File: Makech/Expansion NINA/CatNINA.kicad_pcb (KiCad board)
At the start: 2 copper layers, 22.9 x 30.9 mm, 10 parts, among them J1 ESP, U1 ESP32-WROOM

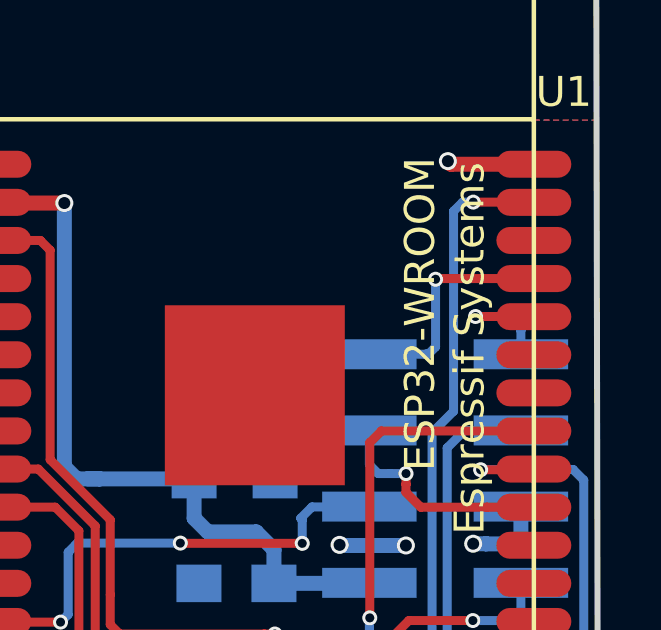
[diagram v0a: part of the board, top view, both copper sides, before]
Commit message: change TX and RX
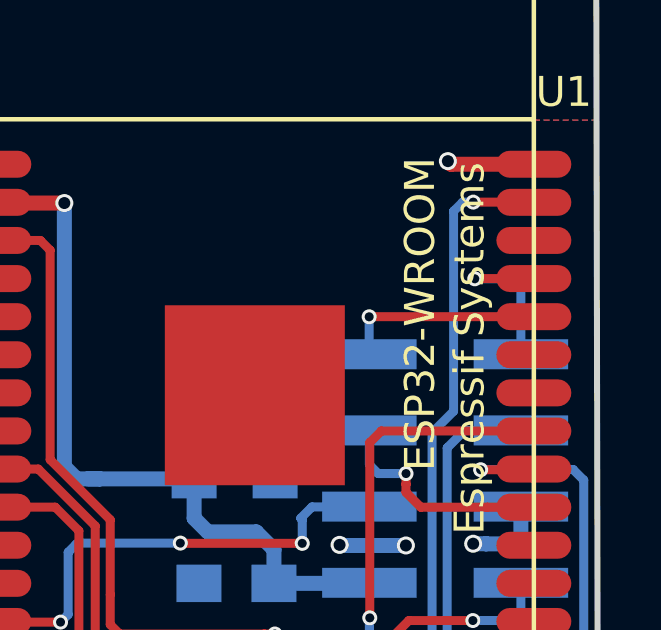
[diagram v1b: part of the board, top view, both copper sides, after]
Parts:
- J1: value ESP -> Conn_02x06_Top_Bottom
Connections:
- J1 pad 1: /ESP_TX -> /ESP_RX
- J1 pad 2: /ESP_RX -> /ESP_TX
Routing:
- net /ESP_RX: track 4.60 -> 6.74 mm
- net /ESP_TX: track 7.88 -> 5.81 mm
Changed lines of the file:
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@@
     (thickness 1.6)
     (drawings 50)
-    (tracks 159)
+    (tracks 153)
     (zones 0)
     (modules 10)
@@
   )
   (layers
-    (0 F.Cu signal hide)
-    (31 B.Cu signal hide)
+    (0 F.Cu signal)
+    (31 B.Cu signal)
     (32 B.Adhes user)
     (33 F.Adhes user)
@@
       (effects (font (size 1 1) (thickness 0.15)) (justify mirror))
     )
-    (fp_text value ESP (at 5.34416 -0.17018 270) (layer B.Fab)
+    (fp_text value Conn_02x06_Top_Bottom (at 5.34416 -0.17018 270) (layer B.Fab)
       (effects (font (size 1 1) (thickness 0.15)) (justify mirror))
     )
@@
     )
     (pad 2 smd rect (at -2.525 6.35 180) (size 3.15 1) (layers B.Cu B.Paste B.Mask)
-      (net 30 /ESP_RX))
-    (pad 1 smd rect (at 2.525 6.35 180) (size 3.15 1) (layers B.Cu B.Paste B.Mask)
       (net 29 /ESP_TX))
+    (pad 1 smd rect (at 2.525 6.35 180) (size 3.15 1) (layers B.Cu B.Paste B.Mask)
+      (net 30 /ESP_RX))
     (pad 4 smd rect (at -2.525 3.81 180) (size 3.15 1) (layers B.Cu B.Paste B.Mask)
       (net 25 /ESP_GPIO0))
@@
   (segment (start 155.88488 113.59134) (end 164.87648 113.59134) (width 0.3) (layer F.Cu) (net 28))
   (segment (start 164.87648 113.59134) (end 165.9255 112.54232) (width 0.3) (layer F.Cu) (net 28))
-  (segment (start 170.0692 101.16566) (end 170.09188 101.14298) (width 0.3) (layer F.Cu) (net 29))
-  (segment (start 166.48478 103.66502) (end 166.48732 103.66248) (width 0.3) (layer B.Cu) (net 29))
-  (segment (start 164.60978 103.66502) (end 166.48478 103.66502) (width 0.3) (layer B.Cu) (net 29))
-  (segment (start 166.48732 103.66248) (end 166.57574 103.66248) (width 0.3) (layer B.Cu) (net 29))
-  (via (at 166.81648 101.16566) (size 0.5) (drill 0.3) (layers F.Cu B.Cu) (net 29))
-  (segment (start 166.57574 103.66248) (end 166.81648 103.42174) (width 0.3) (layer B.Cu) (net 29))
-  (segment (start 166.81648 103.42174) (end 166.81648 101.16566) (width 0.3) (layer B.Cu) (net 29))
-  (segment (start 166.83916 101.14298) (end 166.81648 101.16566) (width 0.3) (layer F.Cu) (net 29))
-  (segment (start 170.09188 101.14298) (end 166.83916 101.14298) (width 0.3) (layer F.Cu) (net 29))
-  (segment (start 169.65978 102.86502) (end 169.66184 102.86296) (width 0.3) (layer B.Cu) (net 30))
-  (segment (start 169.65978 103.66502) (end 169.65978 102.86502) (width 0.3) (layer B.Cu) (net 30))
-  (segment (start 169.66184 102.86296) (end 169.66184 102.60584) (width 0.3) (layer B.Cu) (net 30))
-  (via (at 168.148 102.40772) (size 0.5) (drill 0.3) (layers F.Cu B.Cu) (net 30))
-  (segment (start 169.66184 102.60584) (end 169.46372 102.40772) (width 0.3) (layer B.Cu) (net 30))
-  (segment (start 169.46372 102.40772) (end 168.148 102.40772) (width 0.3) (layer B.Cu) (net 30))
-  (segment (start 170.08662 102.40772) (end 170.09188 102.41298) (width 0.3) (layer F.Cu) (net 30))
-  (segment (start 168.148 102.40772) (end 170.08662 102.40772) (width 0.3) (layer F.Cu) (net 30))
+  (via (at 168.1226 101.15042) (size 0.5) (drill 0.3) (layers F.Cu B.Cu) (net 29))
+  (segment (start 170.09188 101.14298) (end 168.13004 101.14298) (width 0.3) (layer F.Cu) (net 29))
+  (segment (start 168.13004 101.14298) (end 168.1226 101.15042) (width 0.3) (layer F.Cu) (net 29))
+  (segment (start 169.65978 101.51412) (end 169.65978 103.66502) (width 0.3) (layer B.Cu) (net 29))
+  (segment (start 168.1226 101.15042) (end 169.29608 101.15042) (width 0.3) (layer B.Cu) (net 29))
+  (segment (start 169.29608 101.15042) (end 169.65978 101.51412) (width 0.3) (layer B.Cu) (net 29))
+  (via (at 164.60216 102.41788) (size 0.5) (drill 0.3) (layers F.Cu B.Cu) (net 30))
+  (segment (start 170.09188 102.41298) (end 164.60706 102.41298) (width 0.3) (layer F.Cu) (net 30))
+  (segment (start 164.60706 102.41298) (end 164.60216 102.41788) (width 0.3) (layer F.Cu) (net 30))
+  (segment (start 164.60216 103.6574) (end 164.60978 103.66502) (width 0.3) (layer B.Cu) (net 30))
+  (segment (start 164.60216 102.41788) (end 164.60216 103.6574) (width 0.3) (layer B.Cu) (net 30))
   (via (at 165.83152 107.64266) (size 0.5) (drill 0.3) (layers F.Cu B.Cu) (net 31))
   (segment (start 161.4678 107.82046) (end 161.4678 106.7562) (width 0.3) (layer B.Cu) (net 31))

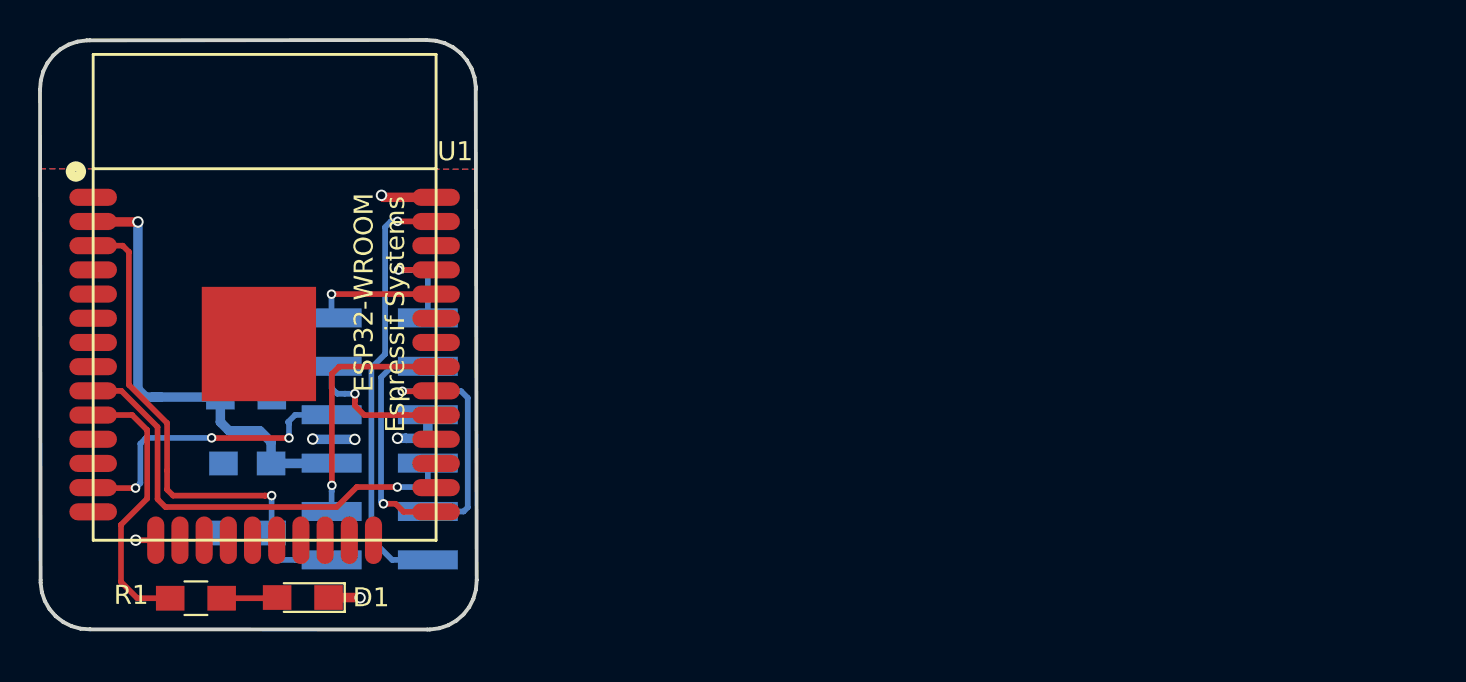
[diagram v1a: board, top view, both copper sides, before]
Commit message: move conector
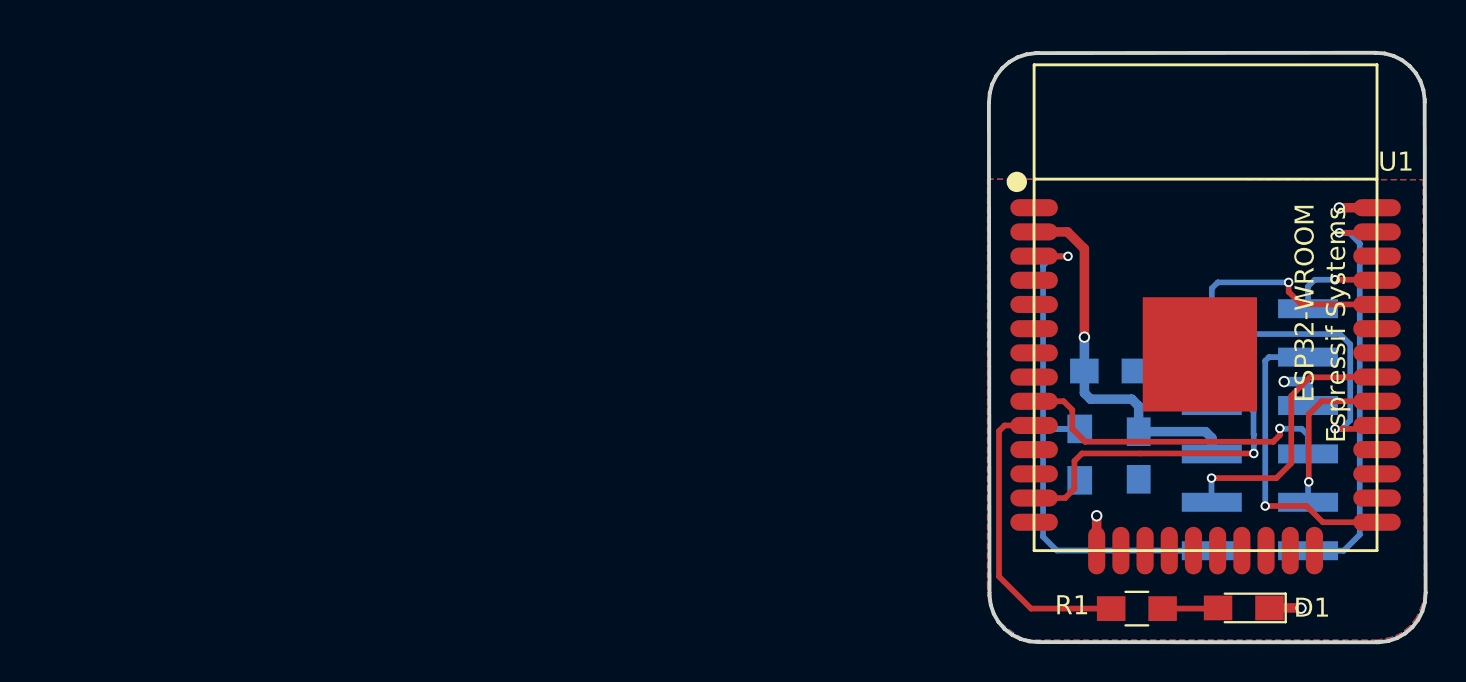
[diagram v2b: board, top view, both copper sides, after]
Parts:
- moved G*** 57.5 mm to (217.8, 95.0)
- moved G*** 52.2 mm to (204.4, 116.8)
- moved G*** 51.3 mm to (203.2, 101.4)
- moved D1 49.4 mm to (212.5, 118.9)
- moved R1 49.4 mm to (206.9, 118.9)
- moved U1 49.4 mm to (210.5, 103.1)
- moved C1 46.8 mm to (207.0, 110.9), turned to 270 degrees
- moved J1 46.2 mm to (213.3, 109.5)
- moved R3 45.4 mm to (205.5, 106.5)
- moved R2 44.0 mm to (203.9, 110.8), turned to 270 degrees
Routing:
- net /ESP_CS: track 12.0 -> 20.0 mm
- net /ESP_BUSY: track 23.8 -> 17.5 mm
- net +3V3: track 24.8 -> 19.9 mm
- net /ESP_SCK: track 13.3 -> 8.51 mm
- net /ESP_RX: track 6.74 -> 10.6 mm
- net /ESP_GPIO0: track 12.4 -> 16.2 mm
- net GND: track 10.9 -> 7.83 mm, vias 6 -> 4
- net /ESP_RESET: track 27.2 -> 30.0 mm
- net /ESP_MOSI: track 16.0 -> 17.9 mm, vias 3 -> 1
- net /IO25: track 14.6 -> 16.2 mm
- net /ESP_RTS: track 12.9 -> 14.2 mm
- net /ESP_MISO: track 22.9 -> 21.7 mm
- net /ESP_TX: track 5.81 -> 4.95 mm

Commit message: update nina v0.1
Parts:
- removed the G*** at (217.8, 95.0)

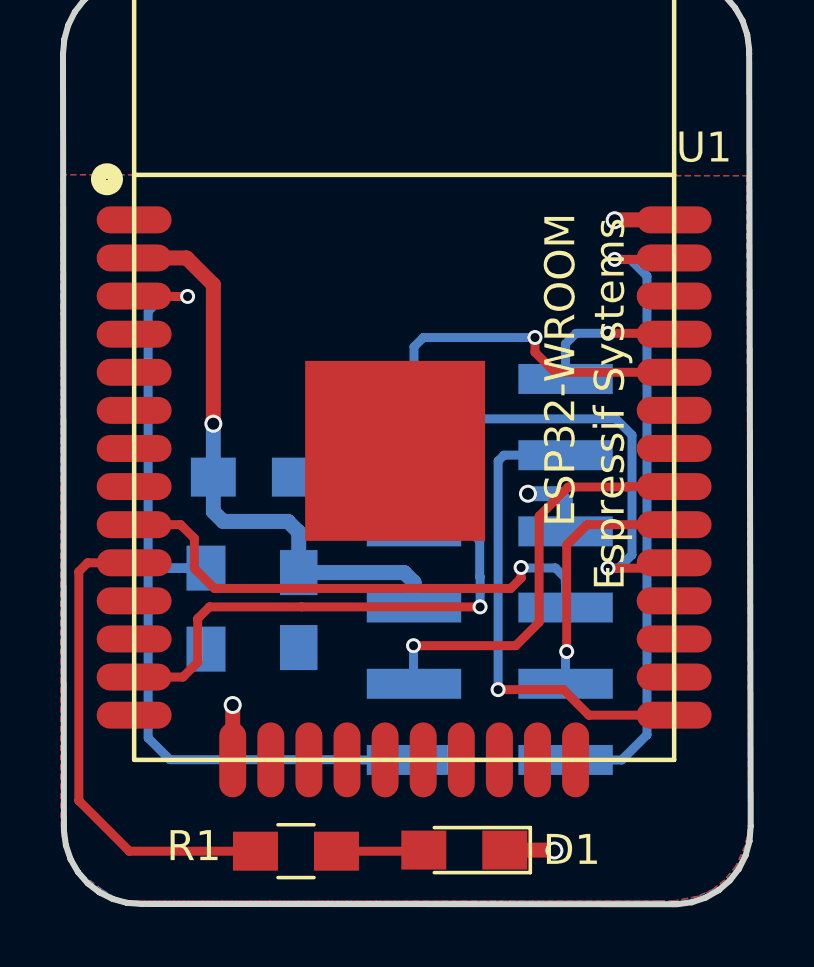
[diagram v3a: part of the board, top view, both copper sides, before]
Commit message: update traces WiFiNINA
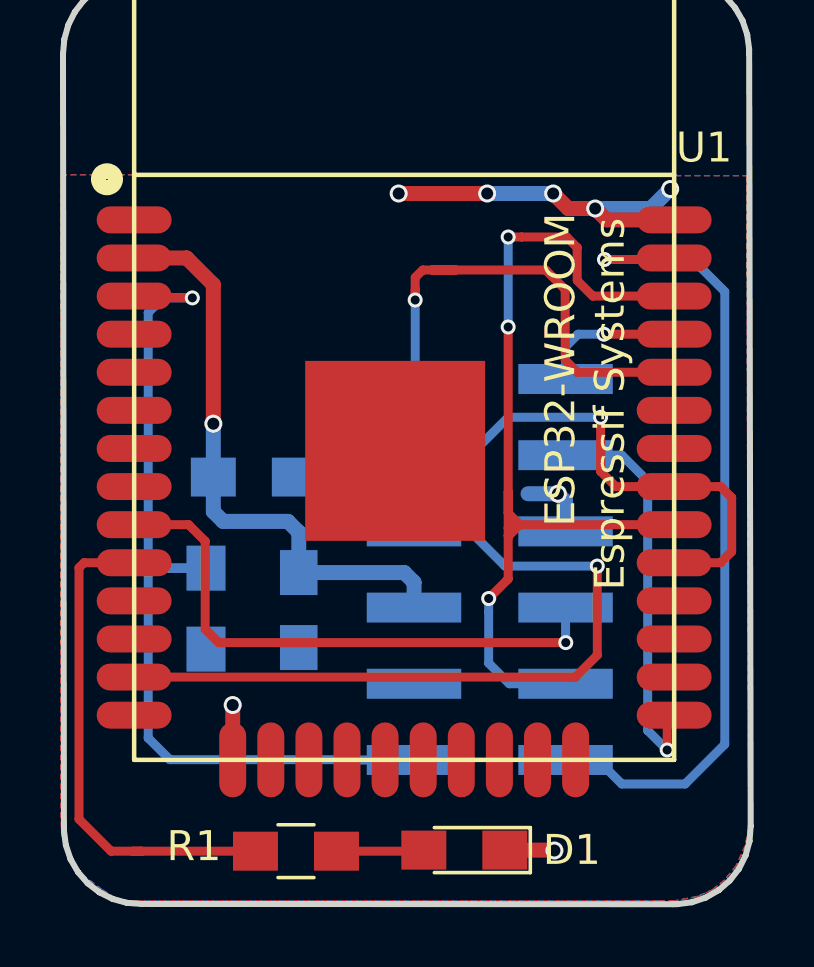
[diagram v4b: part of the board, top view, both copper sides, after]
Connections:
- net /ESP_BUSY renamed /ESP_BUSY_ACK
- net /ESP_MISO renamed /ESP_MISO_RX
- net /ESP_MOSI renamed /ESP_MOSI_TX
- J1 pad 10: /ESP_SCK -> /ESP_SCK_CTS
- J1 pad 3: /ESP_CS -> /ESP_CS_RTS
- J1 pad 9: /ESP_RTS -> Net-(J1-Pad9)
- R3 pad 2: /ESP_CS -> /ESP_CS_RTS
- U1 pad 29: /ESP_CS -> /ESP_CS_RTS
- U1 pad 30: /ESP_SCK -> /ESP_SCK_CTS
- U1 pad 31: /ESP_RTS -> /ESP_CS_RTS
- U1 pad 36: Net-(U1-Pad36) -> /ESP_SCK_CTS
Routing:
- net /ESP_SCK_CTS: track 0.00 -> 31.7 mm, vias 0 -> 3
- net /ESP_CS_RTS: track 0.00 -> 21.4 mm, vias 0 -> 1
- net /ESP_CS: track 20.0 -> 0.00 mm, vias 1 -> 0
- net /ESP_RTS: track 14.2 -> 0.00 mm, vias 1 -> 0
- net GND: track 7.83 -> 18.2 mm, vias 4 -> 8
- net /ESP_SCK: track 8.51 -> 0.00 mm, vias 1 -> 0
- net /ESP_MOSI_TX: track 17.9 -> 25.3 mm
- net /ESP_MISO_RX: track 21.7 -> 28.1 mm
- net /ESP_RX: track 10.6 -> 16.3 mm
- net /ESP_GPIO0: track 16.2 -> 13.6 mm
- net /ESP_BUSY_ACK: track 17.5 -> 18.9 mm
- net /IO25: track 16.2 -> 16.9 mm
- net /ESP_RESET: track 30.0 -> 30.6 mm
